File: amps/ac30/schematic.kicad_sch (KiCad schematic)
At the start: 82 parts, among them J1 1/4 in, J2 1/4 in, J3 1/4 in, J4 1/4 in, J5 1/4 in, J6 1/4 in, SW3 SPST, SW4 DPST, T1 4k a-a, T2 280-0-280 V

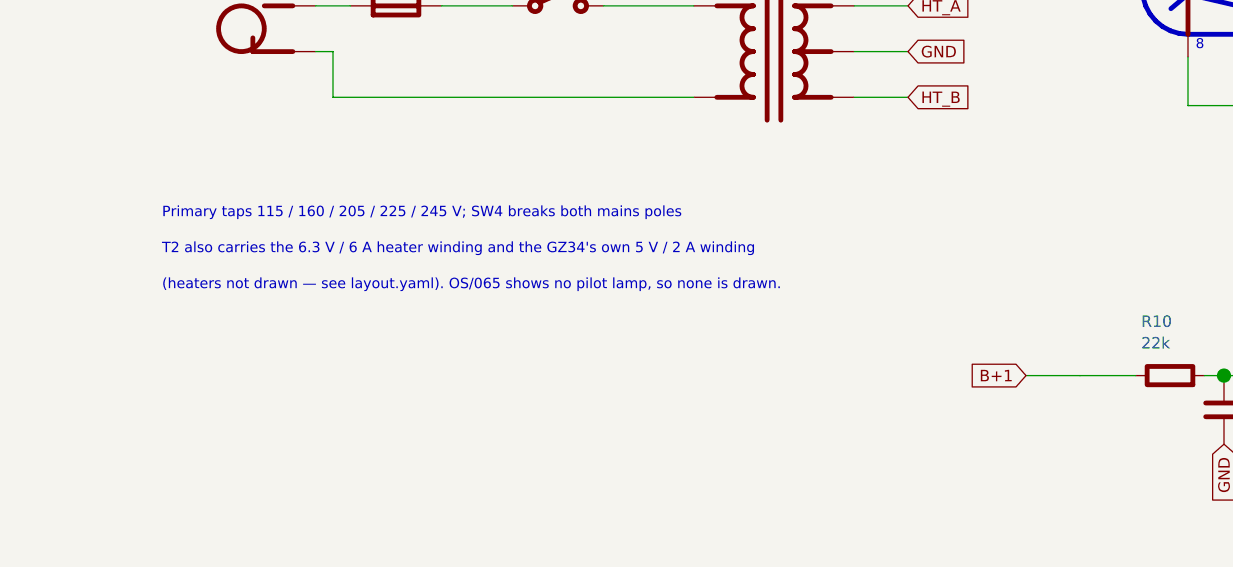
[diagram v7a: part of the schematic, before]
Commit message: Fix: the one sheet note the sweep missed (AC30), and the count the previous message got wrong
63c7f67 said 33 draw scripts; the diff was 36. It also left one string on
the AC30 sheet — "(heaters not drawn — see layout.yaml)" — because the
leftover scan's failure did not stop the commit that followed it. Fixed here;
every sheet outside the three under tone repair now renders no repository
file name. The same sheet note records that the OS/065 drawing shows no
pilot lamp, which is why none is drawn on the AC30 board.

Co-Authored-By: Claude Fable 5.1 <noreply@anthropic.com>
Claude-Session: https://claude.ai/code/session_01KBMfdh37HmCL2iWcBiL5J1
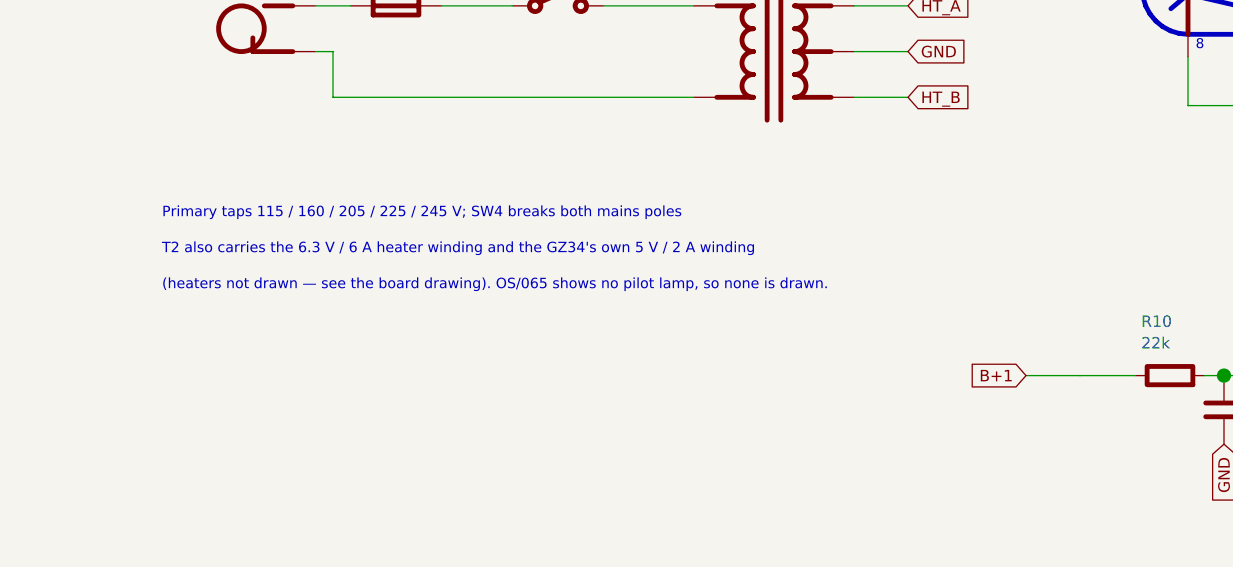
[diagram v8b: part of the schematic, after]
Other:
- note added: "(heaters not drawn — see the board drawing). OS/065 shows no pilot lamp, so none is drawn."
- note removed: "(heaters not drawn — see layout.yaml). OS/065 shows no pilot lamp, so none is drawn."
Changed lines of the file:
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@@
   (text "T2 also carries the 6.3 V / 6 A heater winding and the GZ34's own 5 V / 2 A winding" (at 207.063 247.82 0)
     (effects (font (size 1.15 1.15)) (justify left)))
-  (text "(heaters not drawn — see layout.yaml). OS/065 shows no pilot lamp, so none is drawn." (at 207.063 251.82 0)
+  (text "(heaters not drawn — see the board drawing). OS/065 shows no pilot lamp, so none is drawn." (at 207.063 251.82 0)
     (effects (font (size 1.15 1.15)) (justify left)))
   (global_label "HT_A" (shape input) (at 321.063 205.82 90)
